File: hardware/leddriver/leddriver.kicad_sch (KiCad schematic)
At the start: 0 parts

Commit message: asd
asd
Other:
- added sheet fpga-som (som.kicad_sch)
- added sheet spf (spf.kicad_sch)
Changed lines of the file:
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@@
 	(generator_version "10.0")
 	(paper "A4")
+	(sheet
+		(at 48.26 34.29)
+		(size 34.29 15.24)
+		(exclude_from_sim no)
+		(in_bom yes)
+		(on_board yes)
+		(dnp no)
+		(fields_autoplaced yes)
+		(stroke
+			(width 0.1524)
+			(type solid)
+		)
+		(fill
+			(color 0 0 0 0)
+		)
+		(property "Sheetname" "spf"
+			(at 48.26 33.5784 0)
+			(show_name no)
+			(do_not_autoplace no)
+			(effects
+				(font
+					(size 1.27 1.27)
+				)
+				(justify left bottom)
+			)
+		)
+		(property "Sheetfile" "spf.kicad_sch"
+			(at 48.26 50.1146 0)
+			(show_name no)
+			(do_not_autoplace no)
+			(effects
+				(font
+					(size 1.27 1.27)
+				)
+				(justify left top)
+			)
+		)
+		(instances
+			(project "leddriver"
+				(path "/21fda176-5e39-481b-9f0c-fdef3996088e"
+					(page "3")
+				)
+			)
+		)
+	)
+	(sheet
+		(at 139.7 45.72)
+		(size 44.45 39.37)
+		(exclude_from_sim no)
+		(in_bom yes)
+		(on_board yes)
+		(dnp no)
+		(fields_autoplaced yes)
+		(stroke
+			(width 0.1524)
+			(type solid)
+		)
+		(fill
+			(color 0 0 0 0)
+		)
+		(property "Sheetname" "fpga-som"
+			(at 139.7 45.0084 0)
+			(show_name no)
+			(do_not_autoplace no)
+			(effects
+				(font
+					(size 1.27 1.27)
+				)
+				(justify left bottom)
+			)
+		)
+		(property "Sheetfile" "som.kicad_sch"
+			(at 139.7 85.6746 0)
+			(show_name no)
+			(do_not_autoplace no)
+			(effects
+				(font
+					(size 1.27 1.27)
+				)
+				(justify left top)
+			)
+		)
+		(instances
+			(project "leddriver"
+				(path "/21fda176-5e39-481b-9f0c-fdef3996088e"
+					(page "2")
+				)
+			)
+		)
+	)
 	(sheet_instances
 		(path "/"

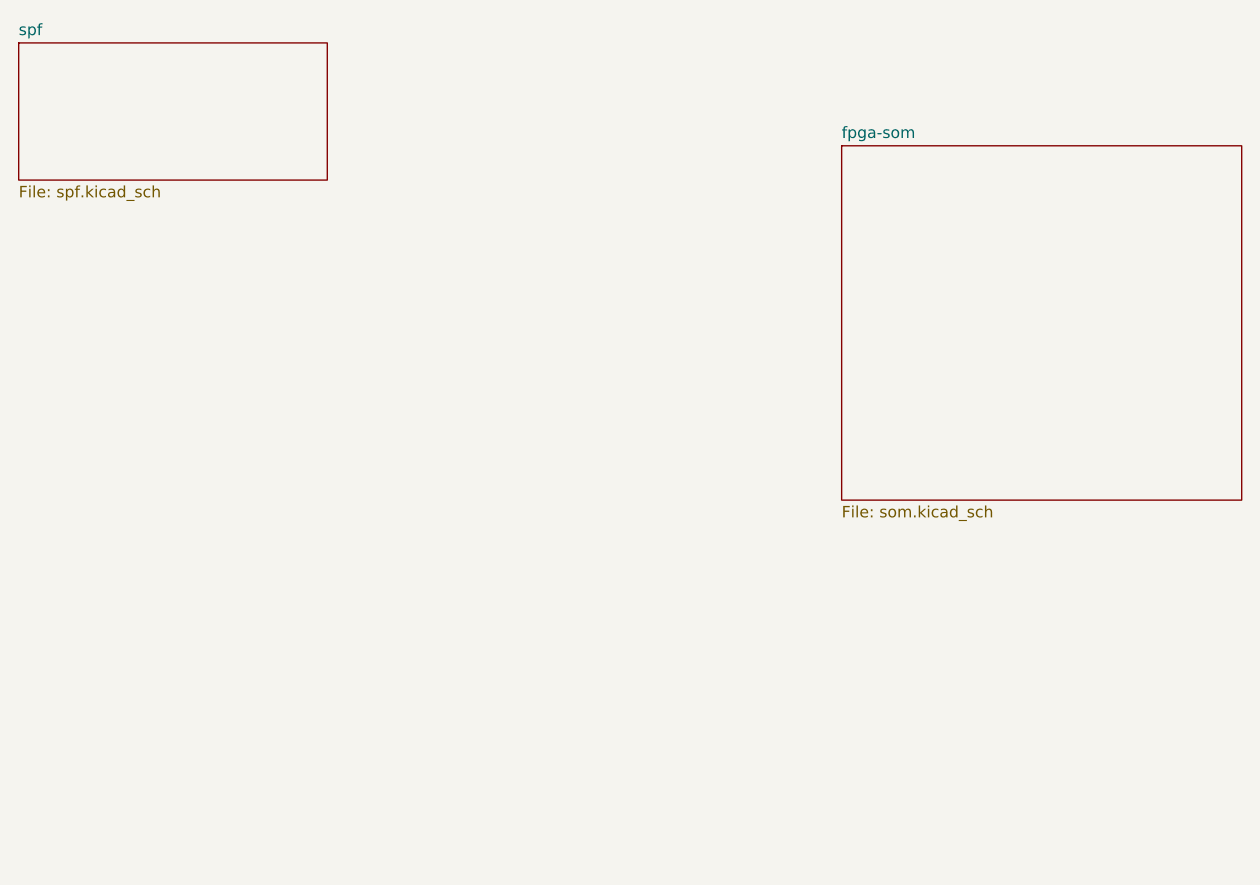
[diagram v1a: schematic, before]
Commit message: driver
started fucking about with the matrix gateware, lost te plot and deleted it
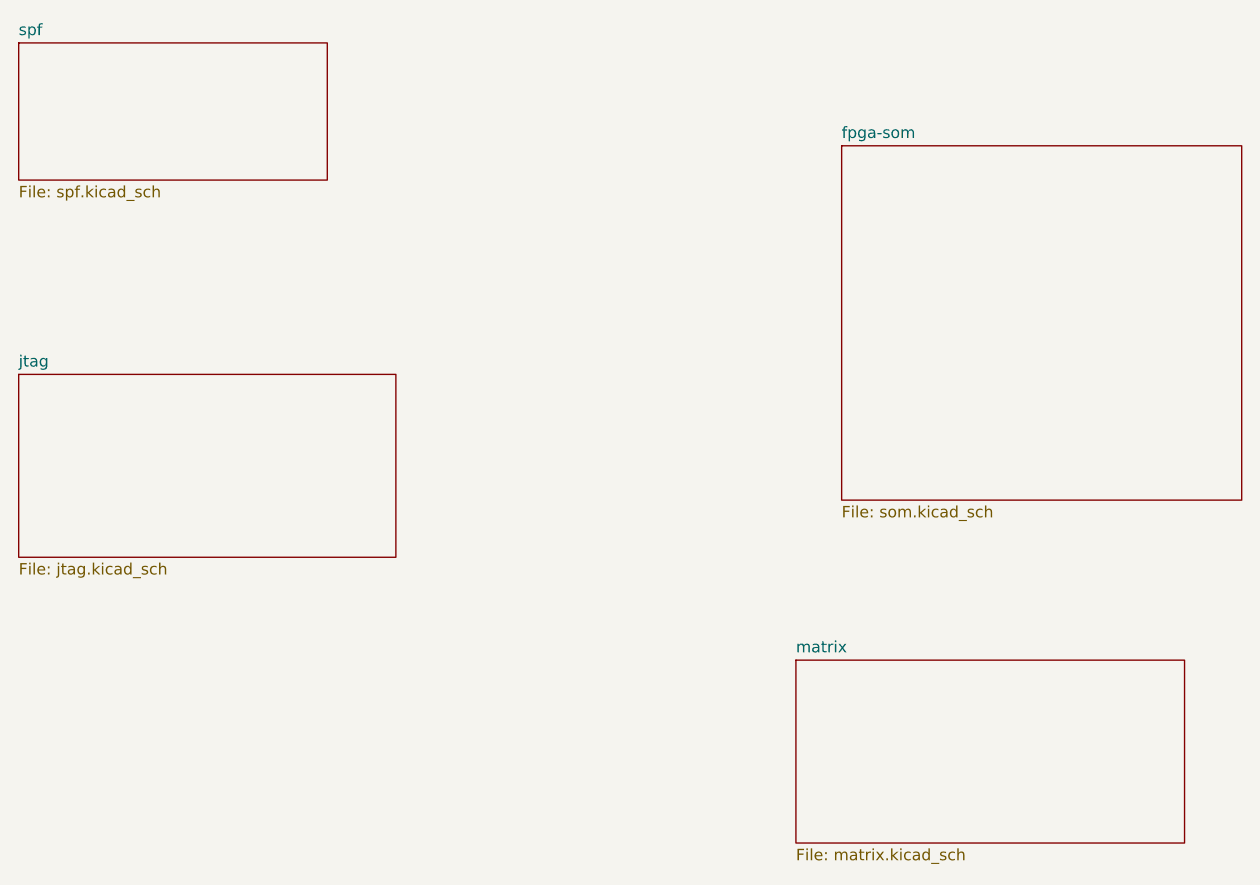
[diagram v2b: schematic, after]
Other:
- added sheet jtag (jtag.kicad_sch)
- added sheet matrix (matrix.kicad_sch)
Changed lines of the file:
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@@
 	(paper "A4")
+	(sheet
+		(at 134.62 102.87)
+		(size 43.18 20.32)
+		(exclude_from_sim no)
+		(in_bom yes)
+		(on_board yes)
+		(dnp no)
+		(fields_autoplaced yes)
+		(stroke
+			(width 0.1524)
+			(type solid)
+		)
+		(fill
+			(color 0 0 0 0)
+		)
+		(property "Sheetname" "matrix"
+			(at 134.62 102.1584 0)
+			(show_name no)
+			(do_not_autoplace no)
+			(effects
+				(font
+					(size 1.27 1.27)
+				)
+				(justify left bottom)
+			)
+		)
+		(property "Sheetfile" "matrix.kicad_sch"
+			(at 134.62 123.7746 0)
+			(show_name no)
+			(do_not_autoplace no)
+			(effects
+				(font
+					(size 1.27 1.27)
+				)
+				(justify left top)
+			)
+		)
+		(instances
+			(project "leddriver"
+				(path "/21fda176-5e39-481b-9f0c-fdef3996088e"
+					(page "5")
+				)
+			)
+		)
+	)
 	(sheet
 		(at 48.26 34.29)
@@
 				)
 			)
+		)
+	)
+	(sheet
+		(at 48.26 71.12)
+		(size 41.91 20.32)
+		(exclude_from_sim no)
+		(in_bom yes)
+		(on_board yes)
+		(dnp no)
+		(fields_autoplaced yes)
+		(stroke
+			(width 0.1524)
+			(type solid)
+		)
+		(fill
+			(color 0 0 0 0)
+		)
+		(property "Sheetname" "jtag"
+			(at 48.26 70.4084 0)
+			(show_name no)
+			(do_not_autoplace no)
+			(effects
+				(font
+					(size 1.27 1.27)
+				)
+				(justify left bottom)
+			)
+		)
+		(property "Sheetfile" "jtag.kicad_sch"
+			(at 48.26 92.0246 0)
+			(show_name no)
+			(do_not_autoplace no)
+			(effects
+				(font
+					(size 1.27 1.27)
+				)
+				(justify left top)
+			)
+		)
+		(instances
+			(project "leddriver"
+				(path "/21fda176-5e39-481b-9f0c-fdef3996088e"
+					(page "4")
+				)
+			)
